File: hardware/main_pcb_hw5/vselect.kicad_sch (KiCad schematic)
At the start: 5 parts

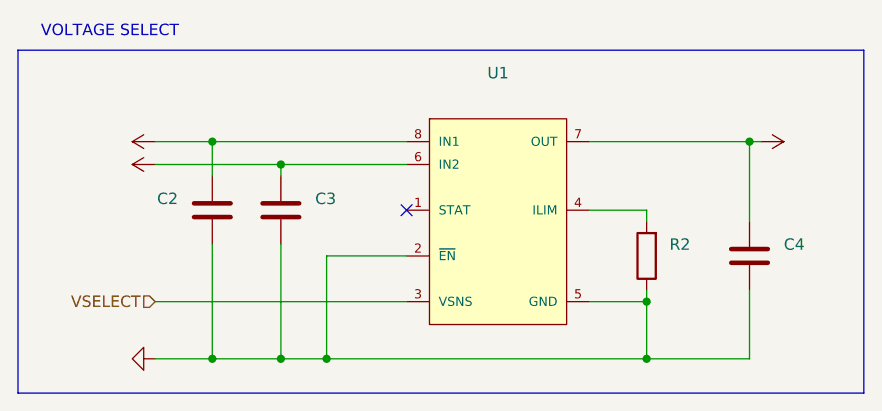
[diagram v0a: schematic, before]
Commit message: HW5 Main PCB, Revision 5
* Migrated files to KiCad 7
* Added RTC
  * IC: Analog Devices Inc. DS3231MZ
  * Battery holder (CR1616): Keystone Electronics 3012
* Cleaned up traces
* Changed ground fill to solid
* Removed test pads and LCD solder jumper
* Cleaned up/prettified silkscreen and logo
* Cleaned up some footprints (more to come eventually)
* Added 3D models for board display
* Schematic image is now a PDF since it has 2 pages
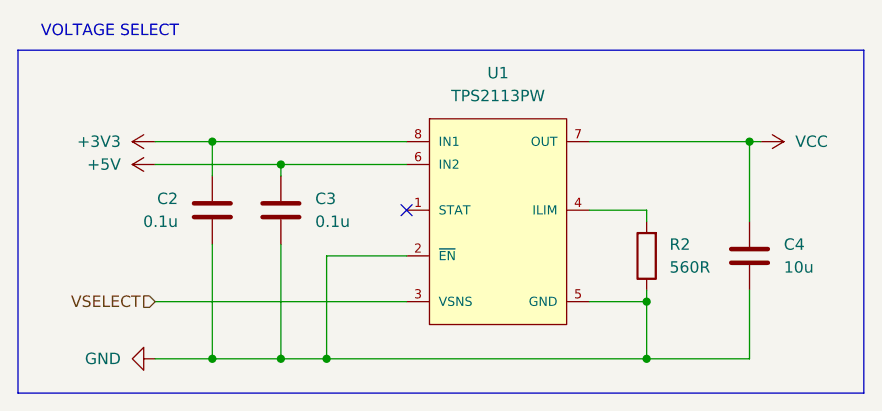
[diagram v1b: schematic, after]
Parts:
- C2, C3: value (none) -> 0.1u; footprint (none) -> Capacitor_SMD:C_0402_1005Metric_Pad0.74x0.62mm_HandSolder
- C4: value (none) -> 10u; footprint (none) -> Capacitor_SMD:C_0402_1005Metric_Pad0.74x0.62mm_HandSolder
- R2: value (none) -> 560R; footprint (none) -> Resistor_SMD:R_0402_1005Metric_Pad0.72x0.64mm_HandSolder
- U1: value (none) -> TPS2113PW; footprint (none) -> Personal:Texas_Instruments-TPS2113PW-Level_A
